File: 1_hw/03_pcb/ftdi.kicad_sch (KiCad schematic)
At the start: 32 parts

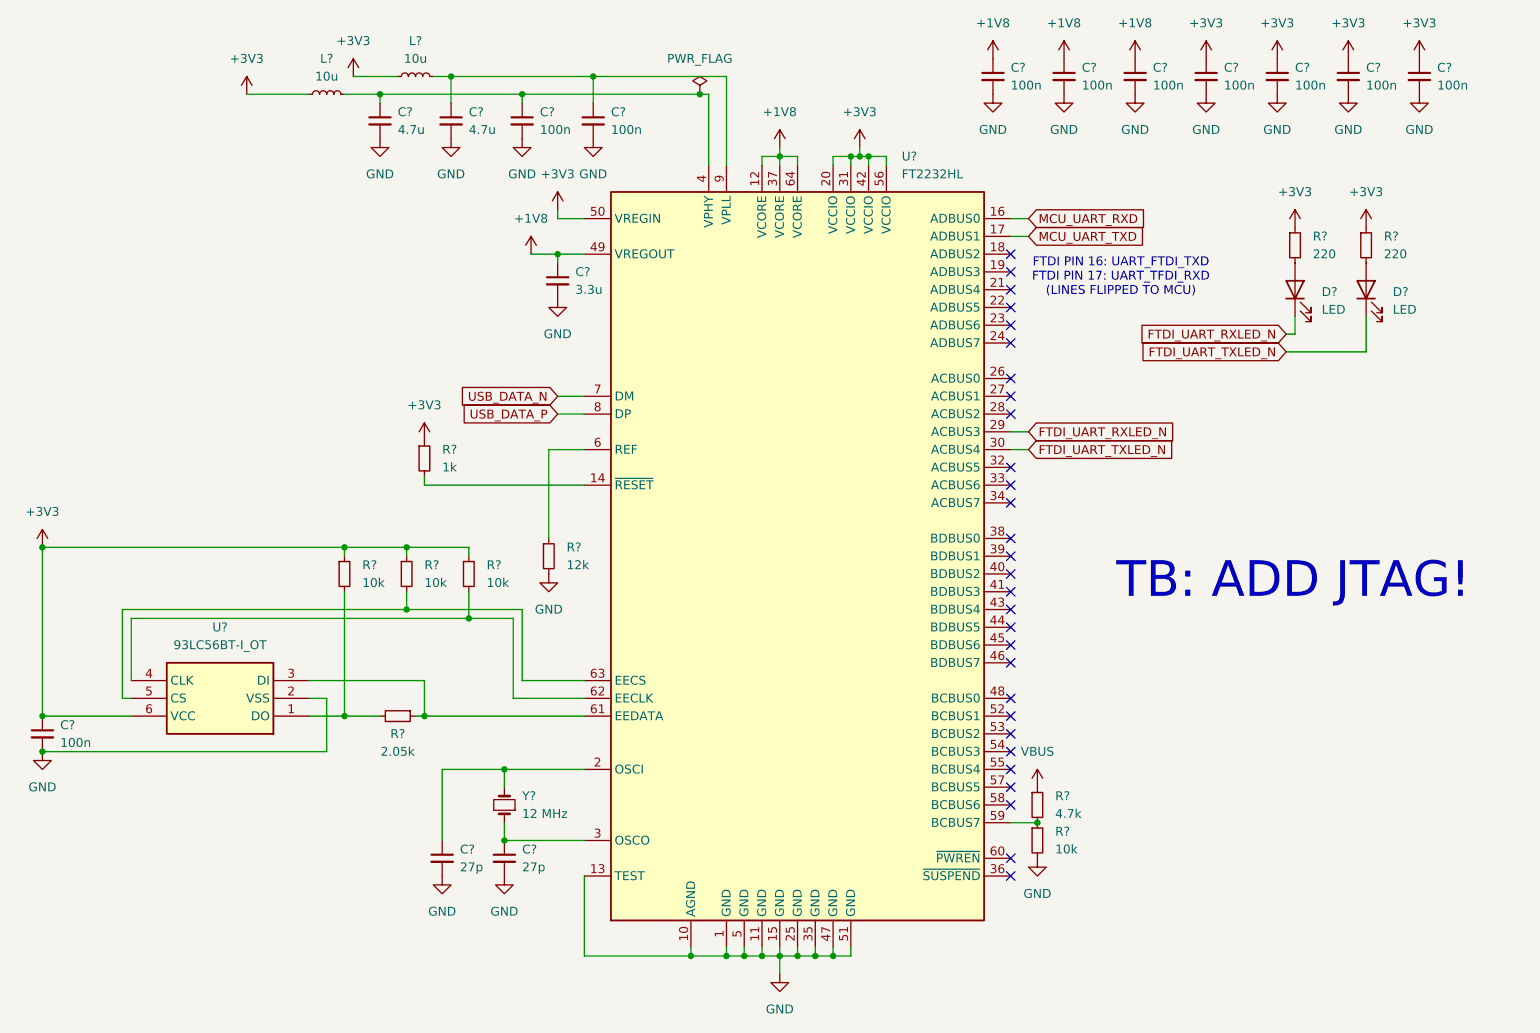
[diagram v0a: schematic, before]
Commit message: FEAT: Finished Excel Pin Map for MCU. Completed MCU + FPGA in Schematic.
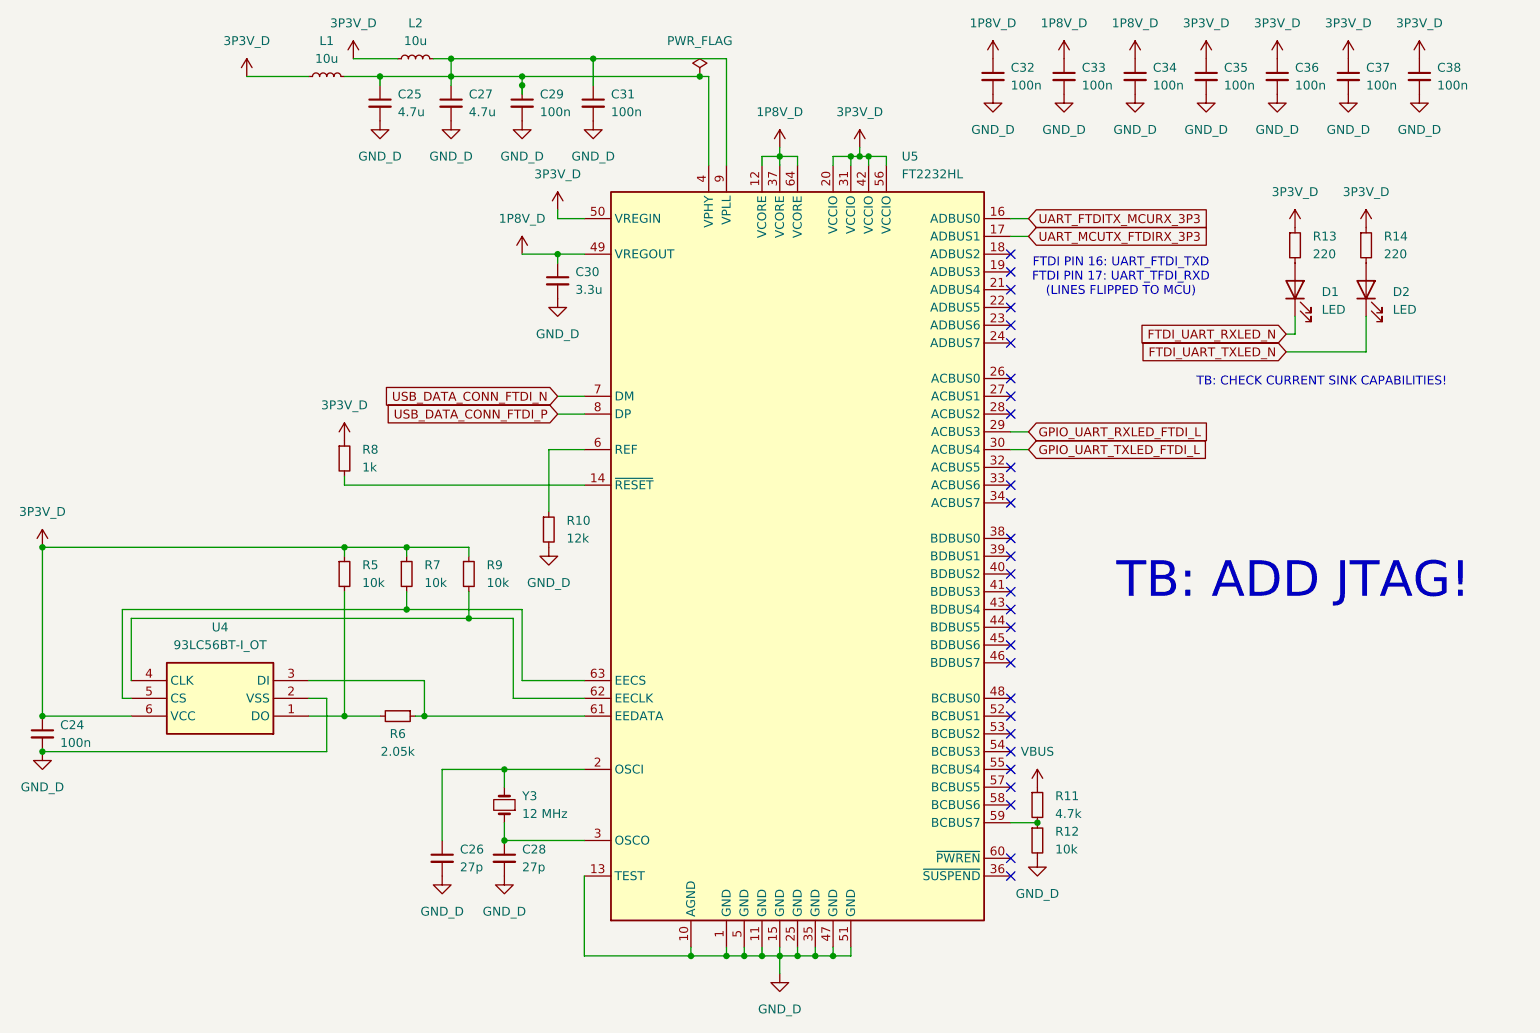
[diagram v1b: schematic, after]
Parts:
- gave numbers to parts that had none: 32
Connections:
- net FTDI_UART_RXLED_N: no longer U5.29 (ACBUS3)
- net FTDI_UART_TXLED_N: no longer U5.30 (ACBUS4)
- net at C25.1, C29.1, L1.2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: now also C27.1, C31.1, L2.2, U5.9 (VPLL)
- net +1V8 renamed 1P8V_D
- net +3V3 renamed 3P3V_D
- net GND renamed GND_D
- net MCU_UART_RXD renamed UART_FTDITX_MCURX_3P3
- net MCU_UART_TXD renamed UART_MCUTX_FTDIRX_3P3
- net USB_DATA_N renamed USB_DATA_CONN_FTDI_N
- net USB_DATA_P renamed USB_DATA_CONN_FTDI_P
- new net GPIO_UART_RXLED_FTDI_L: U5.29 (ACBUS3)
- new net GPIO_UART_TXLED_FTDI_L: U5.30 (ACBUS4)
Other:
- note added: "TB: CHECK CURRENT SINK CAPABILITIES!"
- moved on the sheet: C25, C27, C29, C31, L1, L2, R10, R8

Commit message: FEAT: Added FTDI JTAG. Added 0 Ohm JTAG Resistors. Added Boot Select Switches.
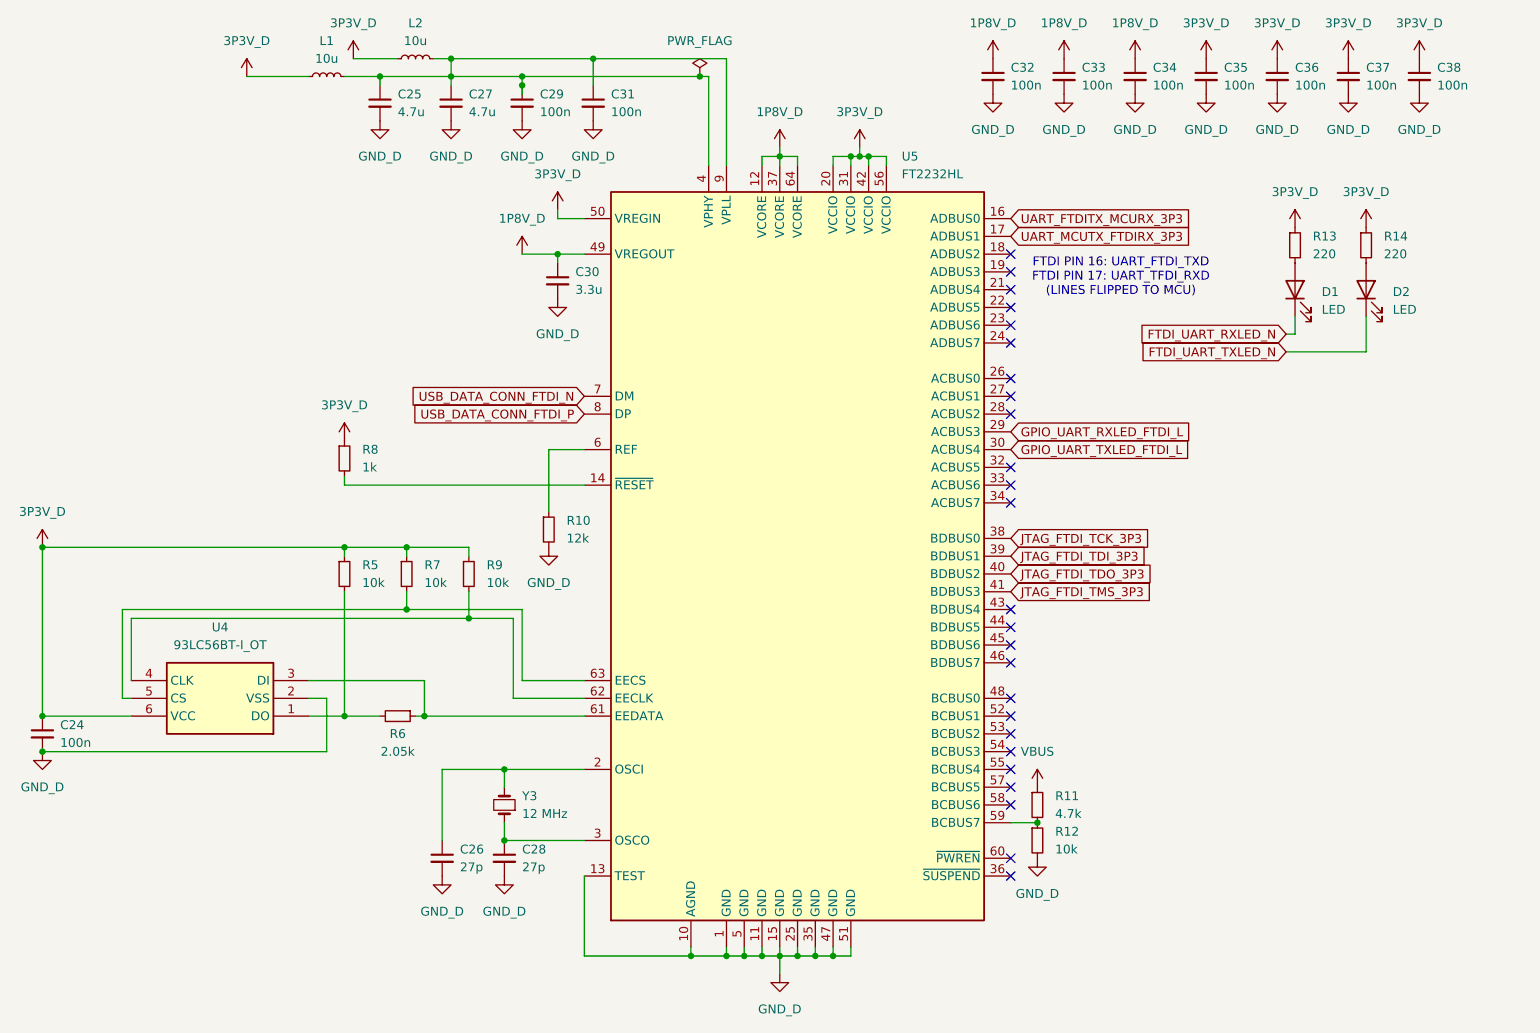
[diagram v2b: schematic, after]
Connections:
- net JTAG_FTDI_TCK_3P3: now reaches U5.38 (BDBUS0)
- net JTAG_FTDI_TDI_3P3: now reaches U5.39 (BDBUS1)
- net JTAG_FTDI_TDO_3P3: now reaches U5.40 (BDBUS2)
- net JTAG_FTDI_TMS_3P3: now reaches U5.41 (BDBUS3)
- no-connect marks 29 -> 25
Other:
- note removed: "TB: ADD JTAG!"
- note removed: "TB: CHECK CURRENT SINK CAPABILITIES!"
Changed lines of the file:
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@@
-	)
-	(no_connect
-		(at 182.88 105.41)
 	)
 	(no_connect
@@
 	)
 	(no_connect
-		(at 182.88 100.33)
-	)
-	(no_connect
 		(at 182.88 67.31)
 	)
@@
 	)
 	(no_connect
-		(at 182.88 107.95)
-	)
-	(no_connect
 		(at 182.88 115.57)
 	)
@@
 	)
 	(no_connect
-		(at 182.88 102.87)
-	)
-	(no_connect
 		(at 182.88 130.81)
 	)
@@
 	(wire
 		(pts
-			(xy 118.11 82.55) (xy 121.92 82.55)
-		)
-		(stroke
-			(width 0)
-			(type default)
-		)
-	)
-	(wire
-		(pts
 			(xy 73.66 34.29) (xy 82.55 34.29)
 		)
@@
 	(wire
 		(pts
-			(xy 182.88 85.09) (xy 185.42 85.09)
-		)
-		(stroke
-			(width 0)
-			(type default)
-		)
-	)
-	(wire
-		(pts
 			(xy 96.52 110.49) (xy 55.88 110.49)
 		)
@@
 	(wire
 		(pts
-			(xy 182.88 87.63) (xy 185.42 87.63)
-		)
-		(stroke
-			(width 0)
-			(type default)
-		)
-	)
-	(wire
-		(pts
 			(xy 101.6 133.35) (xy 101.6 143.51)
 		)
@@
 	(wire
 		(pts
-			(xy 182.88 57.15) (xy 185.42 57.15)
-		)
-		(stroke
-			(width 0)
-			(type default)
-		)
-	)
-	(wire
-		(pts
 			(xy 113.03 120.65) (xy 113.03 110.49)
 		)
@@
 	(wire
 		(pts
-			(xy 118.11 80.01) (xy 121.92 80.01)
-		)
-		(stroke
-			(width 0)
-			(type default)
-		)
-	)
-	(wire
-		(pts
 			(xy 87.63 107.95) (xy 87.63 125.73)
 		)
@@
 	(wire
 		(pts
-			(xy 182.88 54.61) (xy 185.42 54.61)
-		)
-		(stroke
-			(width 0)
-			(type default)
-		)
-	)
-	(wire
-		(pts
 			(xy 139.7 34.29) (xy 139.7 46.99)
 		)
@@
 			(width 0)
 			(type default)
-		)
-	)
-	(text "TB: ADD JTAG!"
-		(exclude_from_sim no)
-		(at 223.266 106.426 0)
-		(effects
-			(font
-				(size 5.08 5.08)
-				(color 255 0 0 1)
-			)
-		)
-	)
-	(text "TB: CHECK CURRENT SINK CAPABILITIES!"
-		(exclude_from_sim no)
-		(at 227.33 77.978 0)
-		(effects
-			(font
-				(size 1.27 1.27)
-				(color 194 0 0 1)
-			)
 		)
 	)
@@
 		)
 	)
-	(global_label "UART_MCUTX_FTDIRX_3P3"
+	(global_label "JTAG_FTDI_TMS_3P3"
 		(shape input)
-		(at 185.42 57.15 0)
+		(at 182.88 107.95 0)
 		(fields_autoplaced yes)
 		(effects
@@
 		)
 		(property "Intersheetrefs" "${INTERSHEET_REFS}"
-			(at 212.2932 57.15 0)
+			(at 204.3103 107.95 0)
 			(effects
 				(font
@@
 		)
 	)
-	(global_label "GPIO_UART_TXLED_FTDI_L"
+	(global_label "UART_MCUTX_FTDIRX_3P3"
 		(shape input)
-		(at 185.42 87.63 0)
+		(at 182.88 57.15 0)
 		(fields_autoplaced yes)
 		(effects
@@
 		)
 		(property "Intersheetrefs" "${INTERSHEET_REFS}"
-			(at 211.9909 87.63 0)
+			(at 209.7532 57.15 0)
+			(effects
+				(font
+					(size 1.27 1.27)
+				)
+				(justify left)
+				(hide yes)
+			)
+		)
+	)
+	(global_label "GPIO_UART_TXLED_FTDI_L"
+		(shape input)
+		(at 182.88 87.63 0)
+		(fields_autoplaced yes)
+		(effects
+			(font
+				(size 1.27 1.27)
+			)
+			(justify left)
+		)
+		(property "Intersheetrefs" "${INTERSHEET_REFS}"
+			(at 209.4509 87.63 0)
 			(effects
 				(font
@@
 	(global_label "UART_FTDITX_MCURX_3P3"
 		(shape input)
-		(at 185.42 54.61 0)
+		(at 182.88 54.61 0)
 		(fields_autoplaced yes)
 		(effects
@@
 		)
 		(property "Intersheetrefs" "${INTERSHEET_REFS}"
-			(at 212.2932 54.61 0)
+			(at 209.7532 54.61 0)
 			(effects
 				(font
@@
 		)
 	)
-	(global_label "USB_DATA_CONN_FTDI_P"
+	(global_label "JTAG_FTDI_TCK_3P3"
 		(shape input)
-		(at 118.11 82.55 180)
+		(at 182.88 100.33 0)
 		(fields_autoplaced yes)
 		(effects
@@
 				(size 1.27 1.27)
 			)
+			(justify left)
+		)
+		(property "Intersheetrefs" "${INTERSHEET_REFS}"
+			(at 204.1894 100.33 0)
+			(effects
+				(font
+					(size 1.27 1.27)
+				)
+				(justify left)
+				(hide yes)
+			)
+		)
+	)
+	(global_label "USB_DATA_CONN_FTDI_P"
+		(shape input)
+		(at 121.92 82.55 180)
+		(fields_autoplaced yes)
+		(effects
+			(font
+				(size 1.27 1.27)
+			)
 			(justify right)
 		)
 		(property "Intersheetrefs" "${INTERSHEET_REFS}"
-			(at 92.5671 82.55 0)
+			(at 96.3771 82.55 0)
 			(effects
 				(font
@@
 	(global_label "GPIO_UART_RXLED_FTDI_L"
 		(shape input)
-		(at 185.42 85.09 0)
+		(at 182.88 85.09 0)
 		(fields_autoplaced yes)
 		(effects
@@
 		)
 		(property "Intersheetrefs" "${INTERSHEET_REFS}"
-			(at 212.2933 85.09 0)
+			(at 209.7533 85.09 0)
+			(effects
+				(font
+					(size 1.27 1.27)
+				)
+				(justify left)
+				(hide yes)
+			)
+		)
+	)
+	(global_label "JTAG_FTDI_TDI_3P3"
+		(shape input)
+		(at 182.88 102.87 0)
+		(fields_autoplaced yes)
+		(effects
+			(font
+				(size 1.27 1.27)
+			)
+			(justify left)
+		)
+		(property "Intersheetrefs" "${INTERSHEET_REFS}"
+			(at 203.5242 102.87 0)
 			(effects
 				(font
@@
 	(global_label "USB_DATA_CONN_FTDI_N"
 		(shape input)
-		(at 118.11 80.01 180)
+		(at 121.92 80.01 180)
 		(fields_autoplaced yes)
 		(effects
@@
 		)
 		(property "Intersheetrefs" "${INTERSHEET_REFS}"
-			(at 92.5066 80.01 0)
+			(at 96.3166 80.01 0)
 			(effects
 				(font
@@
 				(hide yes)
 			)
+		)
+	)
+	(global_label "JTAG_FTDI_TDO_3P3"
+		(shape input)
+		(at 182.88 105.41 0)
+		(fields_autoplaced yes)
+		(effects
+			(font
+				(size 1.27 1.27)
+			)
+			(justify left)
+		)
+		(property "Intersheetrefs" "${INTERSHEET_REFS}"
+			(at 204.2499 105.41 0)
+			(effects
+				(font
+					(size 1.27 1.27)
+				)
+				(justify left)
+				(hide yes)
+			)

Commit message: FEAT: Simulated Analog Paths, added first stage analog amp to schematic.
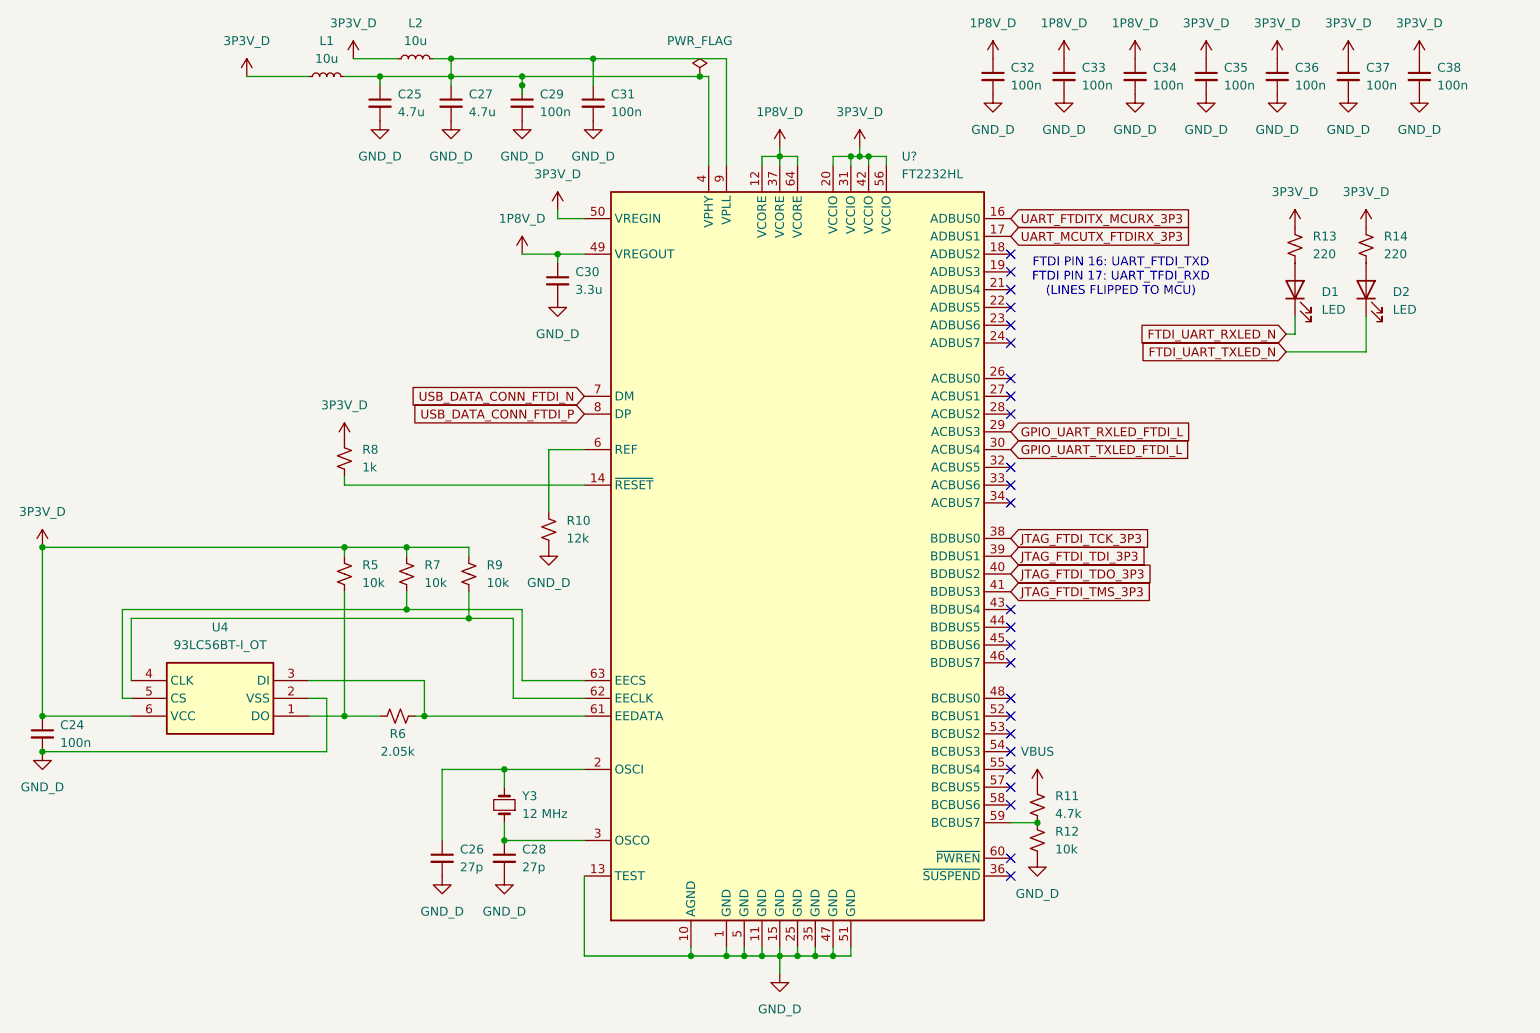
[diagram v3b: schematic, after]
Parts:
- removed U5: FT2232HL, Package_QFP:LQFP-64_10x10mm_P0.5mm, symbol Interface_USB:FT2232HL
- added U?: FT2232HL, Package_QFP:LQFP-64_10x10mm_P0.5mm, symbol BRZK_FTDI:FT2232HL
- R10, R11, R12, R13, R14, R5, R6, R7, R8, R9: symbol Device:R_Small -> Device:R_Small_US
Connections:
- net 1P8V_D: now also U?.12 (VCORE), U?.37 (VCORE), U?.49 (VREGOUT), U?.64 (VCORE)
- net 3P3V_D: now also U?.20 (VCCIO), U?.31 (VCCIO), U?.42 (VCCIO), U?.50 (VREGIN), U?.56 (VCCIO)
- net GND_D: now also U?.1 (GND), U?.10 (AGND), U?.11 (GND), U?.13 (TEST), U?.15 (GND), U?.25 (GND), U?.35 (GND), U?.47 (GND), U?.5 (GND), U?.51 (GND)
- net GPIO_UART_RXLED_FTDI_L: now also U?.29 (ACBUS3)
- net GPIO_UART_TXLED_FTDI_L: now also U?.30 (ACBUS4)
- net JTAG_FTDI_TCK_3P3: now also U?.38 (BDBUS0)
- net JTAG_FTDI_TDI_3P3: now also U?.39 (BDBUS1)
- net JTAG_FTDI_TDO_3P3: now also U?.40 (BDBUS2)
- net JTAG_FTDI_TMS_3P3: now also U?.41 (BDBUS3)
- net UART_FTDITX_MCURX_3P3: now also U?.16 (ADBUS0)
- net UART_MCUTX_FTDIRX_3P3: now also U?.17 (ADBUS1)
- net USB_DATA_CONN_FTDI_N: now also U?.7 (DM)
- net USB_DATA_CONN_FTDI_P: now also U?.8 (DP)
- net at R10.1: now also U?.6 (REF)
- net at C28.1, Y3.1: now also U?.3 (OSCO)
- net at C26.1, Y3.2: now also U?.2 (OSCI)
- net at C25.1, C27.1, C29.1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: now also U?.4 (VPHY), U?.9 (VPLL)
- net at R9.2, U4.4 (CLK): now also U?.62 (EECLK)
- net at R7.2, U4.5 (CS): now also U?.63 (EECS)
- net at R8.2: now also U?.14 (~{RESET})
- net at R11.2, R12.1: now also U?.59 (BCBUS7)
- net at R6.1, U4.3 (DI): now also U?.61 (EEDATA)
